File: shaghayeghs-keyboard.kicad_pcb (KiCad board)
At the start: 2 copper layers, 80 x 119 mm, 47 parts, among them J1 DISPLAY, SW1 SW_Push, SW10 SW_Push, SW11 SW_Push, SW12 SW_Push, SW13 SW_Push, SW14 SW_Push, SW15 RotaryEncoder_Switch, SW16 RotaryEncoder_Switch, SW2 SW_Push, SW3 SW_Push, SW4 SW_Push, SW5 SW_Push, SW6 SW_Push, SW7 SW_Push, SW8 SW_Push, SW9 SW_Push, U1 Sparkfun_Pro_Micro

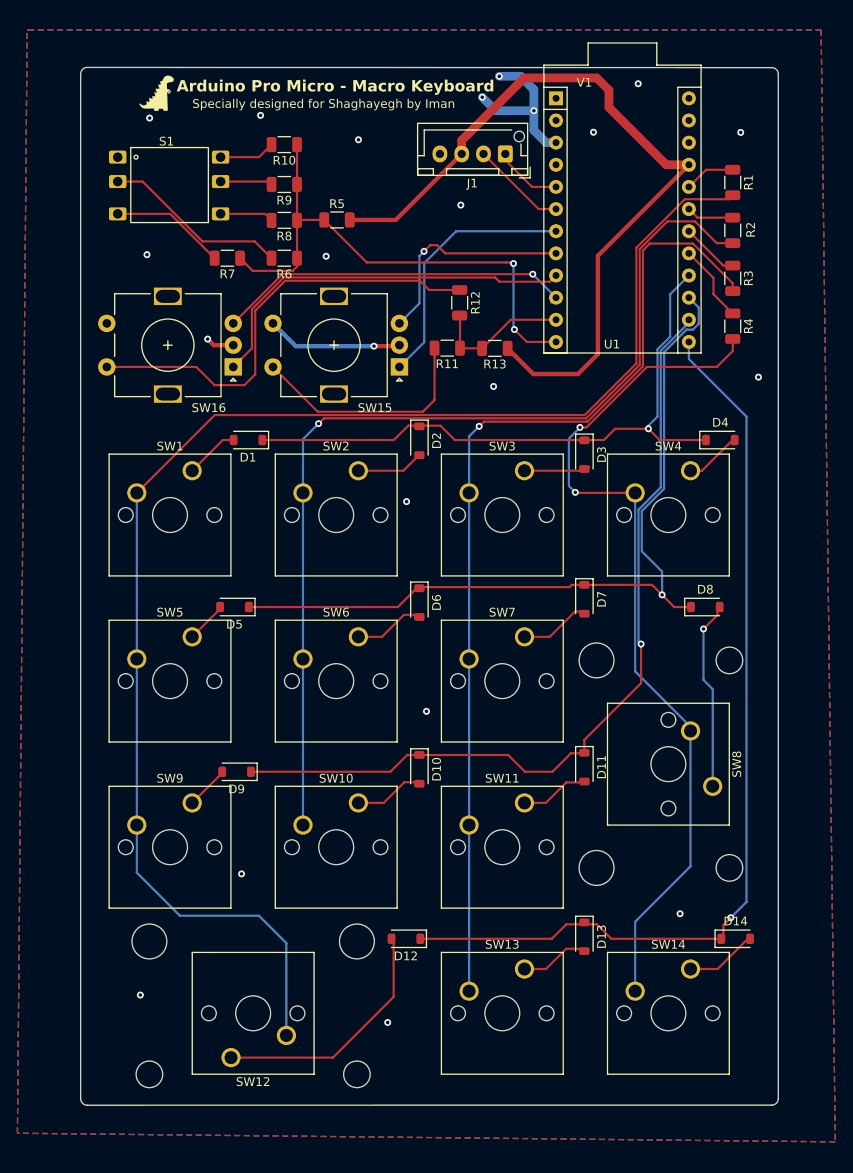
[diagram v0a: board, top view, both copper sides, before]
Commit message: First STM32 design
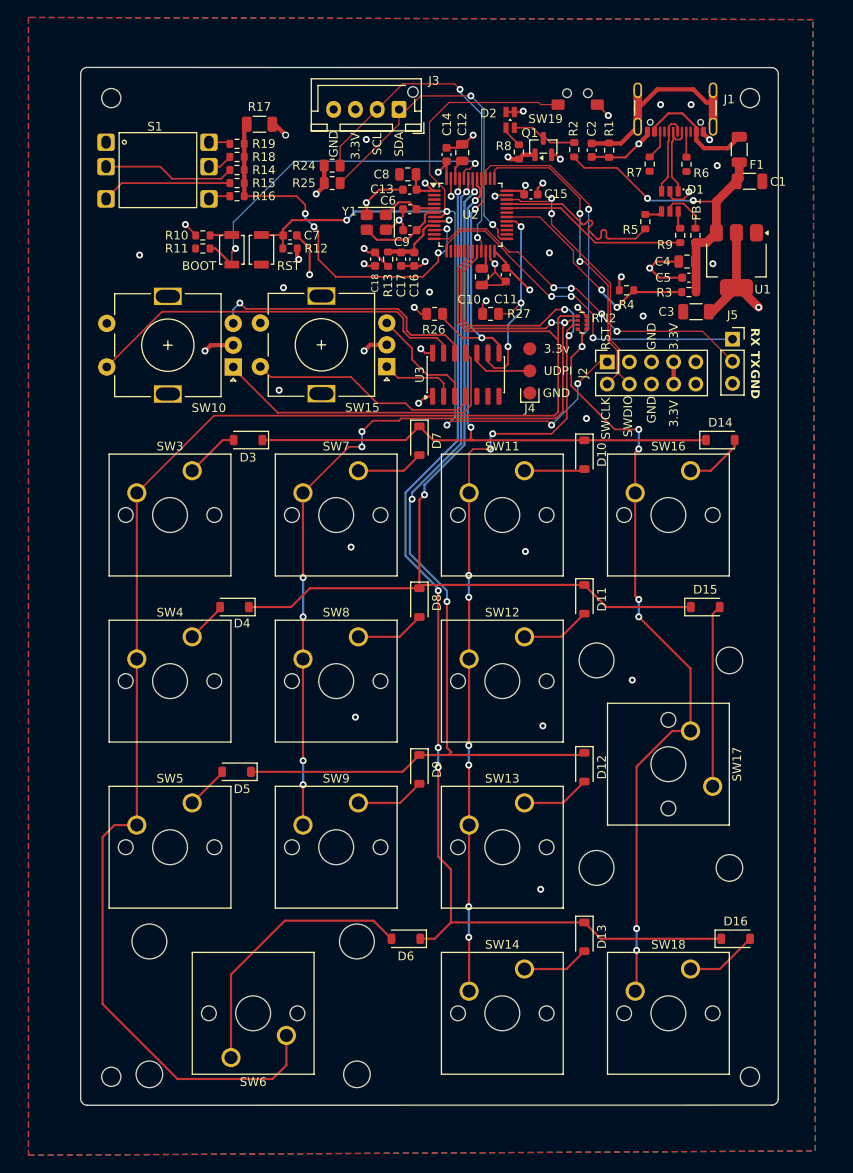
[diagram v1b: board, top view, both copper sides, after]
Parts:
- added C1: 10u, Capacitor_SMD:C_1206_3216Metric, F.Cu at (157.7, 51.0)
- added C10: 2.2u, Capacitor_SMD:C_0805_2012Metric, F.Cu at (127.0, 62.0)
- added C11: 100n, Capacitor_SMD:C_0603_1608Metric, F.Cu at (129.8, 61.8)
- added C12: 2.2u, Capacitor_SMD:C_0805_2012Metric, F.Cu at (124.8, 47.8)
- added C13: 100n, Capacitor_SMD:C_0603_1608Metric, F.Cu at (118.7, 52.0)
- added C14: 100n, Capacitor_SMD:C_0603_1608Metric, F.Cu at (123.0, 48.0)
- added C15: 100n, Capacitor_SMD:C_0603_1608Metric, F.Cu at (132.6, 52.5)
- added C16: 100n, Capacitor_SMD:C_0603_1608Metric, F.Cu at (119.2, 60.0)
- added C17: 1u, Capacitor_SMD:C_0603_1608Metric, F.Cu at (117.8, 60.0)
- added C18: 1u, Capacitor_SMD:C_0603_1608Metric, F.Cu at (114.8, 60.0)
- added C2: 4.7nF, Capacitor_SMD:C_0603_1608Metric, F.Cu at (139.6, 47.5)
- added C3: 22u, Capacitor_SMD:C_1206_3216Metric, F.Cu at (151.6, 66.0)
- added C4: 4.7u, Capacitor_SMD:C_0805_2012Metric, F.Cu at (150.5, 60.2)
- added C5: 100n, Capacitor_SMD:C_0603_1608Metric, F.Cu at (150.8, 62.1)
- added C6: 18p, Capacitor_SMD:C_0603_1608Metric, F.Cu at (118.7, 54.2)
- added C7: 100n, Capacitor_SMD:C_0603_1608Metric, F.Cu at (105.0, 57.2)
- added C8: 4.7u, Capacitor_SMD:C_0805_2012Metric, F.Cu at (118.5, 50.2)
- added C9: 18p, Capacitor_SMD:C_0603_1608Metric, F.Cu at (118.8, 56.6)
- added D1: USBLC6-2SC6, digikey-footprints:SOT23-6L, F.Cu at (148.6, 53.3)
- added D2: ON, LED_SMD:LED_Kingbright_APHBM2012_2x1.25mm, F.Cu at (130.2, 44.0)
- added F1: Fuse, Resistor_SMD:R_1206_3216Metric, F.Cu at (156.5, 47.4)
- added FB1: FerriteBead, Resistor_SMD:R_0603_1608Metric, F.Cu at (151.5, 57.2)
- added H1: MountingHole, MountingHole:MountingHole_2.2mm_M2, F.Cu at (157.8, 41.5)
- added H2: MountingHole, MountingHole:MountingHole_2.2mm_M2, F.Cu at (84.5, 41.5)
- added H3: MountingHole, MountingHole:MountingHole_2.2mm_M2, F.Cu at (157.8, 153.8)
- added H4: MountingHole, MountingHole:MountingHole_2.2mm_M2, F.Cu at (84.5, 153.8)
- added J1: USB_C_Receptacle_USB2.0_16P, Connector_USB:USB_C_Receptacle_GCT_USB4105-xx-A_16P_TopMnt_Horizontal, F.Cu at (149.2, 41.7)
- added J2: Conn_02x05_Odd_Even, Connector_PinSocket_2.54mm:PinSocket_2x05_P2.54mm_Vertical, F.Cu at (141.4, 71.8)
- added J4: Conn_01x03_Pin, TestPoint:TestPoint_3Pads_Pitch2.54mm_Drill0.7mm, F.Cu at (132.5, 75.3)
- added J5: UART, Connector_PinSocket_2.54mm:PinSocket_1x03_P2.54mm_Vertical, F.Cu at (155.8, 69.2)
- added Q1: SS8050, Package_TO_SOT_SMD:SOT-23, F.Cu at (134.1, 47.1)
- added R10: 10K, Resistor_SMD:R_0603_1608Metric, F.Cu at (95.0, 57.2)
- added R24: 4K7, Resistor_SMD:R_0805_2012Metric, F.Cu at (109.8, 49.2)
- added R25: 4K7, Resistor_SMD:R_0805_2012Metric, F.Cu at (109.8, 51.2)
- added R26: 4K7, Resistor_SMD:R_0805_2012Metric, F.Cu at (121.6, 66.2)
- added R27: 4K7, Resistor_SMD:R_0805_2012Metric, F.Cu at (128.0, 66.2)
- added R5: 0R, Resistor_SMD:R_0603_1608Metric, F.Cu at (145.8, 55.7)
- added R6: 5.1K, Resistor_SMD:R_0603_1608Metric, F.Cu at (150.5, 49.1)
- added R7: 5.1K, Resistor_SMD:R_0603_1608Metric, F.Cu at (146.2, 49.1)
- added R8: 1R2, Resistor_SMD:R_0603_1608Metric, F.Cu at (131.2, 47.7)
- added R9: 0R, Resistor_SMD:R_0603_1608Metric, F.Cu at (149.8, 57.2)
- added RN2: 10K, Resistor_SMD:R_Array_Convex_4x0402, F.Cu at (138.5, 67.2)
- added SW1: Reset, Button_Switch_SMD:SW_SPST_B3U-1000P, F.Cu at (101.7, 58.9)
- added SW19: Reset, Library:Tactile Tact Key right angled - Aliexpress, F.Cu at (137.9, 42.3)
- added SW2: Boot, Button_Switch_SMD:SW_SPST_B3U-1000P, F.Cu at (98.3, 58.9)
- added U2: STM32H523CCTx, Package_QFP:LQFP-48_7x7mm_P0.5mm, F.Cu at (125.7, 54.9)
- added U3: ATtiny804-SS, Package_SO:SOIC-14_3.9x8.7mm_P1.27mm, F.Cu at (125.2, 73.2)
- added Y1: 16MHz, Crystal:Crystal_SMD_3225-4Pin_3.2x2.5mm, F.Cu at (114.9, 55.8)
- Macro keyboard based on STM32H523: renamed from Arduino Pro Micro - Macro Keyboard; moved to B.Cu
- R1: value 10K -> 1M; footprint Resistor_SMD:R_1206_3216Metric -> Resistor_SMD:R_0603_1608Metric
- R11: value 5K -> 10K; footprint Resistor_SMD:R_1206_3216Metric -> Resistor_SMD:R_0603_1608Metric
- R12: footprint Resistor_SMD:R_1206_3216Metric -> Resistor_SMD:R_0603_1608Metric
- R13: value 10K -> 47R; footprint Resistor_SMD:R_1206_3216Metric -> Resistor_SMD:R_0603_1608Metric
- R14: renamed from R6; footprint Resistor_SMD:R_1206_3216Metric -> Resistor_SMD:R_0603_1608Metric
- R15: renamed from R7; footprint Resistor_SMD:R_1206_3216Metric -> Resistor_SMD:R_0603_1608Metric
- R16: renamed from R8; footprint Resistor_SMD:R_1206_3216Metric -> Resistor_SMD:R_0603_1608Metric
- R18: renamed from R9; footprint Resistor_SMD:R_1206_3216Metric -> Resistor_SMD:R_0603_1608Metric
- R19: renamed from R10; footprint Resistor_SMD:R_1206_3216Metric -> Resistor_SMD:R_0603_1608Metric
- R2: value 10K -> 1R5; footprint Resistor_SMD:R_1206_3216Metric -> Resistor_SMD:R_0603_1608Metric
- R3: value 10K -> 33K; footprint Resistor_SMD:R_1206_3216Metric -> Resistor_SMD:R_0603_1608Metric
- R4: value 10K -> 75K; footprint Resistor_SMD:R_1206_3216Metric -> Resistor_SMD:R_0603_1608Metric
- U1: value Sparkfun_Pro_Micro -> AMS1117-3.3; footprint Arduino:Sparkfun_Pro_Micro -> Package_TO_SOT_SMD:SOT-223-3_TabPin2
- moved Macro keyboard based on STM32H523 54.8 mm to (143.8, 49.2), turned to 180 degrees
- moved R11 30.3 mm to (95.0, 58.8), turned to 0 degrees
- moved R12 20.4 mm to (105.0, 58.8), turned to 180 degrees
- moved R2 20.4 mm to (137.6, 47.4)
- moved R13 16.0 mm to (116.2, 60.0), turned to -90 degrees
- moved R1 14.7 mm to (141.6, 47.5), turned to 90 degrees
- moved R17 14.1 mm to (101.5, 44.5)
- moved J3 13.2 mm to (117.5, 42.8)
- moved R4 12.9 mm to (143.6, 63.5), turned to 180 degrees
- moved R14 11.5 mm to (98.9, 49.8)
- moved U1 10.8 mm to (156.2, 60.1), turned to -90 degrees
- moved R15 8.69 mm to (98.9, 51.2)
- moved R18 6.27 mm to (98.9, 48.2)
- moved R16 6.09 mm to (98.9, 52.8)
- moved R19 5.42 mm to (98.9, 46.8)
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- renumbered D3 to D10, D7 to D11, D11 to D12, D4 to D14, D8 to D15, D14 to D16, D1 to D3, D5 to D4, D9 to D5, D12 to D6, D2 to D7, D6 to D8, D10 to D9, J1 to J3, R5 to R17, SW16 to SW10, SW3 to SW11, SW7 to SW12, SW11 to SW13, SW13 to SW14, SW4 to SW16, SW8 to SW17, SW14 to SW18, SW1 to SW3, SW5 to SW4, SW9 to SW5, SW12 to SW6, SW2 to SW7, SW6 to SW8, SW10 to SW9
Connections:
- J3 pad 1: SDA -> OLED_I2C_SDA
- J3 pad 2: CLK -> OLED_I2C_SCL
- J3 pad 3: VCC -> +3.3V
- R1 pad 1: Col1 -> GND
- R1 pad 2: Net-(R1-Pad2) -> /SHILD
- R11 pad 1: A2 -> GND
- R11 pad 2: Net-(R11-Pad2) -> /BOOT
- R12 pad 1: Net-(R12-Pad1) -> +3.3V
- R12 pad 2: A2 -> NRST
- R13 pad 1: VCC -> +3.3VA
- R13 pad 2: A2 -> +3.3V
- R14 pad 1: A1 -> 5WAY_SW
- R15 pad 1: A1 -> 5WAY_SW
- R16 pad 1: A1 -> 5WAY_SW
- R17 pad 1: A1 -> 5WAY_SW
- R17 pad 2: VCC -> +3.3V
- R18 pad 1: A1 -> 5WAY_SW
- R19 pad 1: A1 -> 5WAY_SW
- R2 pad 1: Col2 -> Net-(D2-A1)
- R2 pad 2: Net-(R2-Pad2) -> VBUS
- R3 pad 1: Col3 -> VBUS_SENSING
- R3 pad 2: Net-(R3-Pad2) -> VBUS
- R4 pad 1: Col4 -> VBUS_SENSING
- R4 pad 2: Net-(R4-Pad2) -> GND
- SW10 pad A: E2_A -> Net-(U3-PA1)
- SW10 pad B: E2_B -> Net-(U3-PA2)
- SW10 pad S2: Net-(R12-Pad1) -> Net-(U3-PA3)
- SW11 pad 2: Net-(R3-Pad2) -> Col3
- SW12 pad 2: Net-(R3-Pad2) -> Col3
- SW13 pad 2: Net-(R3-Pad2) -> Col3
- SW14 pad 2: Net-(R3-Pad2) -> Col3
- SW15 pad A: E1_A -> Net-(U3-PA4)
- SW15 pad B: E1_B -> Net-(U3-PA5)
- SW15 pad S2: Net-(R11-Pad2) -> Net-(U3-PA6)
- SW16 pad 2: Net-(R4-Pad2) -> Col4
- SW17 pad 2: Net-(R4-Pad2) -> Col4
- SW18 pad 2: Net-(R4-Pad2) -> Col4
- SW3 pad 2: Net-(R1-Pad2) -> Col1
- SW4 pad 2: Net-(R1-Pad2) -> Col1
- SW5 pad 2: Net-(R1-Pad2) -> Col1
- SW6 pad 2: Net-(R1-Pad2) -> Col1
- SW7 pad 2: Net-(R2-Pad2) -> Col2
- SW8 pad 2: Net-(R2-Pad2) -> Col2
- SW9 pad 2: Net-(R2-Pad2) -> Col2
- U1 pad 1: unconnected-(U1-D1/TX-Pad1) -> GND
- U1 pad 2: unconnected-(U1-D0/RX-Pad2) -> +3.3V
- U1 pad 3: GND -> VBUS
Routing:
- net Col1: track 5.85 -> 176.8 mm
- net Net-(R1-Pad2): track 164.9 -> 0.00 mm
- net Net-(R3-Pad2): track 113.6 -> 0.00 mm, vias 1 -> 0
- net Net-(R2-Pad2): track 112.7 -> 0.00 mm, vias 1 -> 0
- net Col4: track 8.98 -> 119.6 mm, vias 0 -> 8
- net Col3: track 6.66 -> 112.9 mm, vias 0 -> 10
- net NRST: track 0.00 -> 101.4 mm, vias 0 -> 5
- net Col2: track 5.44 -> 106.2 mm, vias 0 -> 8
- net Net-(R4-Pad2): track 100.1 -> 0.00 mm, vias 2 -> 0
- net VCC: track 90.4 -> 0.00 mm
- net A1: track 61.2 -> 0.00 mm, vias 2 -> 0
- net +3.3V: track 0.00 -> 59.4 mm, vias 0 -> 15
- net Net-(R12-Pad1): track 51.0 -> 0.00 mm
- net Net-(U3-PA3): track 0.00 -> 44.7 mm
- net E2_A: track 44.4 -> 0.00 mm
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- added copper zone on In2.Cu, net +3.3V
- added copper zone on In1.Cu, net GND
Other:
- copper layers 2 -> 4
- board text added: "3.3V"
- board text added: "3.3v"
- board text added: "BOOT"
- board text added: "GND"
- board text added: "RST"
- board text added: "RX"
- board text added: "SCL"
- board text added: "SDA"
- board text added: "SWCLK"
- board text added: "SWDIO"
- board text added: "TX"
- board text added: "UDPI"
- board text added: "V2"
- board text removed: "V1"
